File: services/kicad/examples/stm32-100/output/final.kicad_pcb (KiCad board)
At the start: 2 copper layers, 208 x 156 mm, 100 parts, among them J1 5V, U1 STM32F103C8T6, U2 AMS1117-3.3

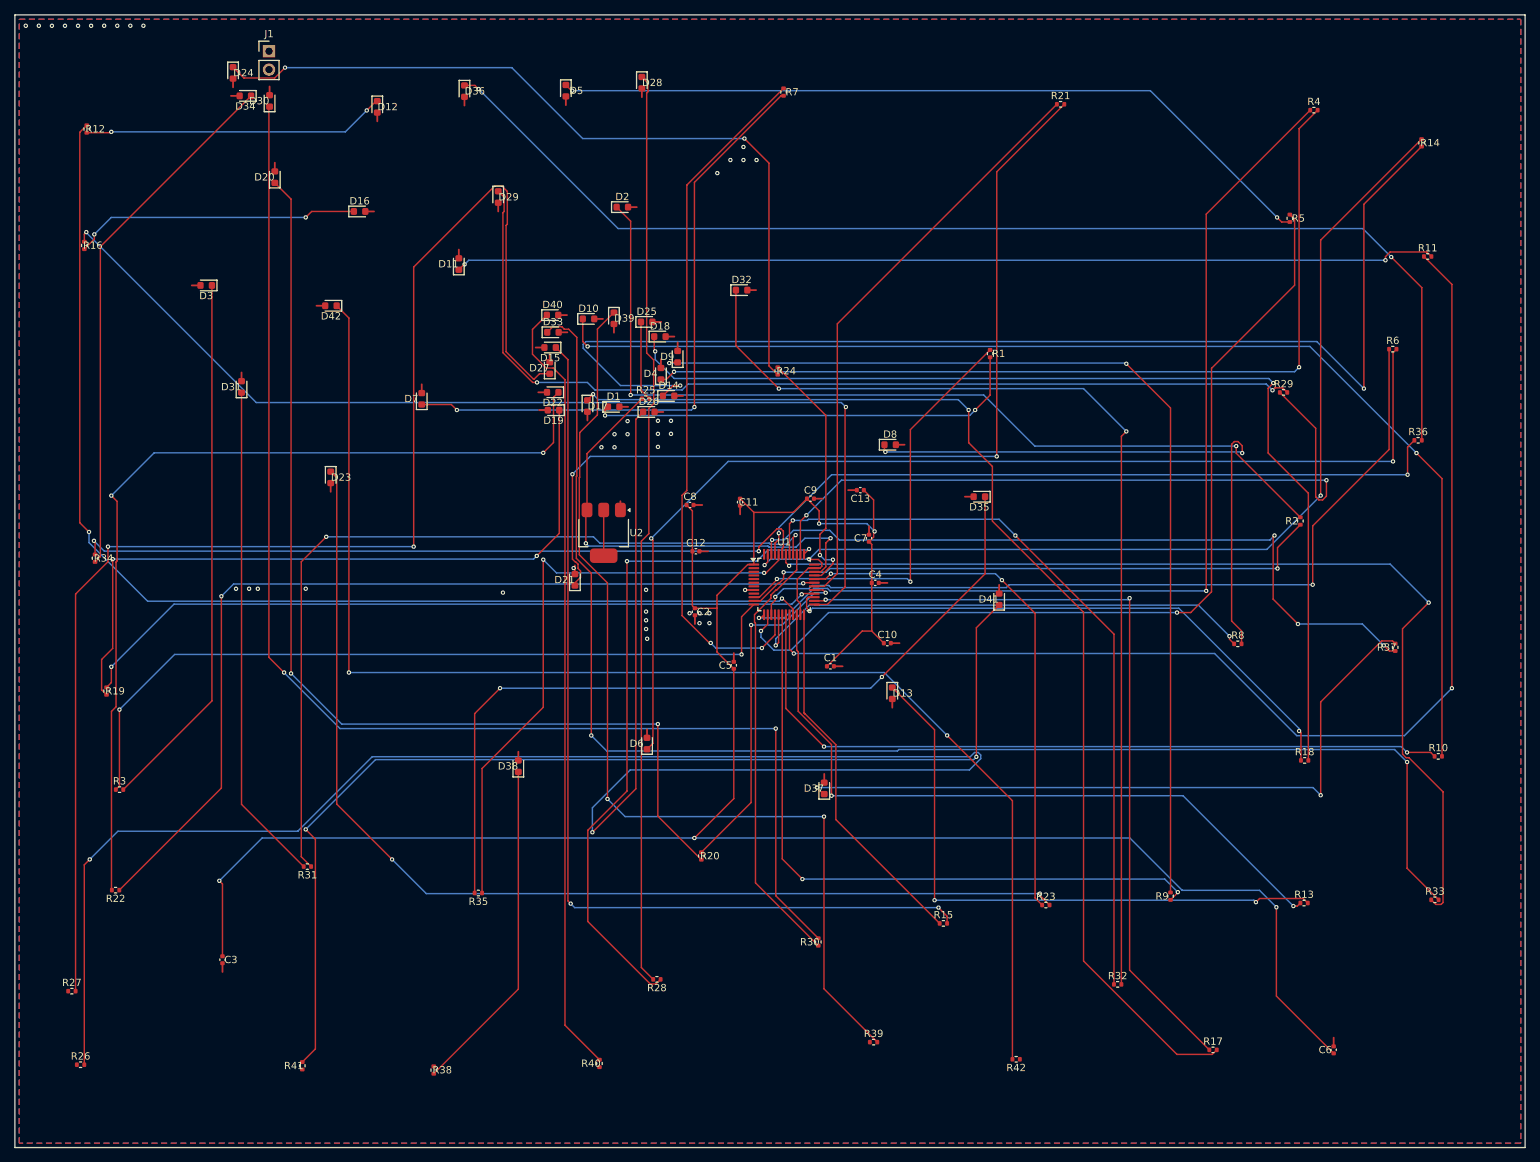
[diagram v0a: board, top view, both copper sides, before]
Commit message: feat(routing): les HUIT cartes du banc a 100 pourcent, 0 erreur, 2 couches
stm32-100, rejouee avec trois tirages complets, ferme :

    stm32-100   100 comp   2 couches   100%   0 manq   0 err   3271 s

Verifie sur le board livre : 0 connexion manquante, 0 erreur. Les 135
avertissements sont de la serigraphie (130) et 5 vias borgnes.

LA CONNEXION MANQUANTE ETAIT UN ACCIDENT DE TIRAGE, pas une propriete de la
carte. Sur le MEME placement gele, Freerouting rend 99, 97, 77, 87 puis 100 —
23 points d ecart sur une carte identique. Un tirage unique n est pas une
mesure, c est un pari ; le banc precedent avait perdu ce pari deux fois de
suite, ce qui m a fait chercher une cause structurelle a l ilot de D21 pendant
des heures. L ilot de 0,9 mm2 etait reel, il n etait simplement pas fatal.

NEVER conclure qu un defaut de routage est structurel sans avoir compte
plusieurs tirages. Le depot le savait pour le PLACEMENT ; la meme prudence vaut
pour le ROUTAGE, et deux tirages concordants ne suffisent pas.

Le banc complet, tous a 100 pourcent / 0 manquante / 0 erreur sur 2 couches :

    arduino-uno 35   esp32-baseline 20   led-blinker 8    nucleo-f401 55
    stm32-30 30      stm32-60 60         stm32-baseline 17   stm32-100 100

Aucune escalade de couches n a servi : le blocage n etait pas un manque de
place, mais des pastilles de masse qu aucun chemin ne reliait au plan.
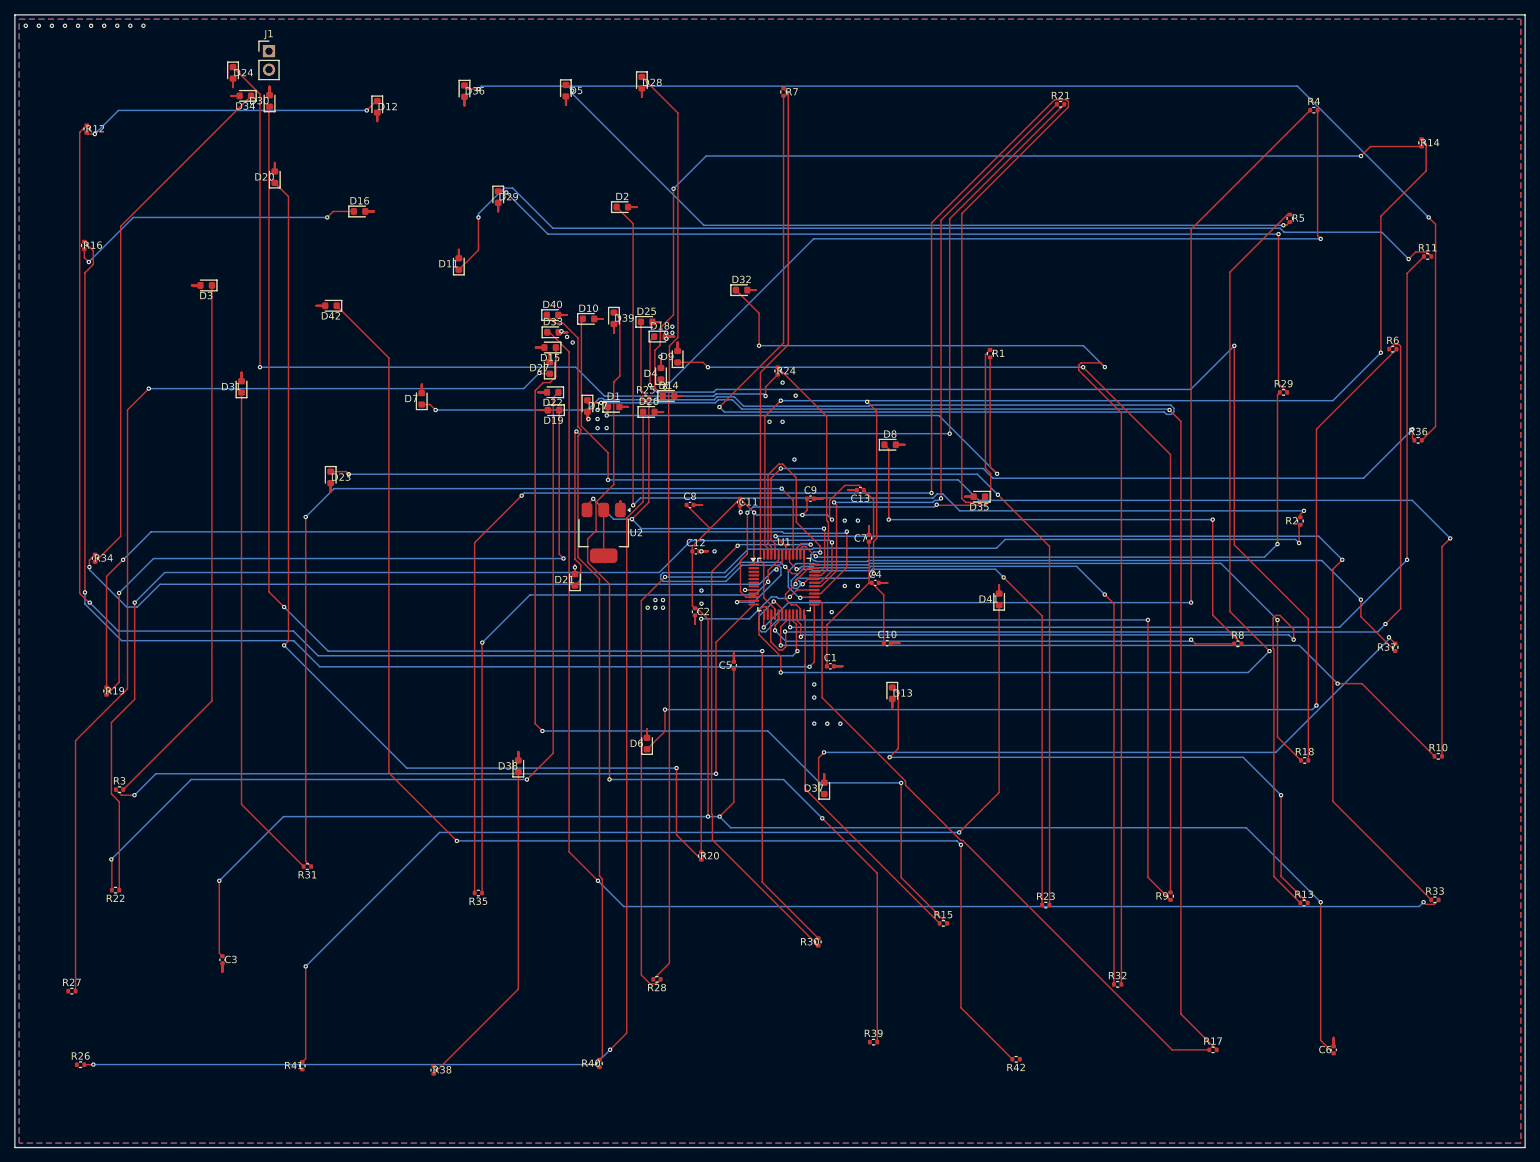
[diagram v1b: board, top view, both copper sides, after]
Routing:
- net GND: track 68.4 -> 273.6 mm, vias 42 -> 50
- net LED9: track 86.2 -> 215.8 mm
- net LED46: track 113.6 -> 241.7 mm
- net LED34: track 278.5 -> 163.0 mm
- net LED35: track 191.6 -> 143.3 mm
- net GPIO2: track 81.8 -> 122.0 mm
- net GPIO18: track 148.7 -> 185.9 mm, vias 3 -> 5
- net GPIO14: track 164.7 -> 133.3 mm
- net LED18: track 166.0 -> 135.5 mm
- net GPIO25: track 104.1 -> 130.9 mm
- net +3V3: track 308.4 -> 334.7 mm, vias 5 -> 7
- net GPIO22: track 110.3 -> 88.0 mm, vias 2 -> 0
- net GPIO9: track 96.6 -> 75.2 mm, vias 2 -> 0
- net GPIO6: track 126.6 -> 146.7 mm
- net GPIO17: track 98.0 -> 117.6 mm
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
